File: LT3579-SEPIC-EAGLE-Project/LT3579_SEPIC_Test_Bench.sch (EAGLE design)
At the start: 3 parts, among them IC1 LT3579EFE#PBF

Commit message: Modified Schematic EAGLE
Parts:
- removed L1: MSD1278T-183MLD, SamacSys_Parts:MSD1278T-183MLD
- added C_1, C_IN_1, C_IN_2, C_OUT_1, C_OUT_2, C_OUT_3: CGA4J1X7R1E475K125AE, SamacSys_Parts:CGA4J1X7R1E475K125AE
- added C_C: CGA4F4C0G2W222J085AE, SamacSys_Parts:CGA4F4C0G2W222J085AE
- added C_F: CGA2B2C0G1H470J050BA, SamacSys_Parts:CGA2B2C0G1H470J050BA
- added C_SS: CGA4J2X8R1E224K125AE, SamacSys_Parts:CGA4J2X8R1E224K125AE
- added L1L2: MSD1278T-183MLD, SamacSys_Parts:MSD1278T-183MLD
- added R_C: AC0805JR-0712KL, SamacSys_Parts:AC0805JR-0712KL
- added R_T: AC0805FR-07124KL, SamacSys_Parts:AC0805FR-07124KL
- added R_UVLO2: RT1206BRD075KL, SamacSys_Parts:RT1206BRD075KL
- added U2: RQ5E050ATTCL, SamacSys_Parts:RQ5E050ATTCL
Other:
- note added: "LT3579 SEPIC Config: 13Vin -> 14Vout"
- moved on the sheet: D1
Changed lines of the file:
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@@
 <layer number="97" name="Info" color="7" fill="1" visible="yes" active="yes"/>
 <layer number="98" name="Guide" color="6" fill="1" visible="yes" active="yes"/>
+<layer number="99" name="SpiceOrder" color="7" fill="1" visible="yes" active="yes"/>
 </layers>
 <schematic xreflabel="%F%N/%S.%C%R" xrefpart="/%S.%C%R">
@@
 <parts>
 <part name="IC1" library="SamacSys_Parts" deviceset="LT3579EFE#PBF" device=""/>
-<part name="L1" library="SamacSys_Parts" deviceset="MSD1278T-183MLD" device=""/>
+<part name="L1L2" library="SamacSys_Parts" deviceset="MSD1278T-183MLD" device=""/>
 <part name="D1" library="SamacSys_Parts" deviceset="MBRS360T3G" device=""/>
+<part name="C_IN_1" library="SamacSys_Parts" deviceset="CGA4J1X7R1E475K125AE" device=""/>
+<part name="C_IN_2" library="SamacSys_Parts" deviceset="CGA4J1X7R1E475K125AE" device=""/>
+<part name="C_1" library="SamacSys_Parts" deviceset="CGA4J1X7R1E475K125AE" device=""/>
+<part name="X_1" library="ngspice-simulation" library_urn="urn:adsk.eagle:library:527439" deviceset="GND" device=""/>
+<part name="X_2" library="ngspice-simulation" library_urn="urn:adsk.eagle:library:527439" deviceset="GND" device=""/>
+<part name="C_OUT_1" library="SamacSys_Parts" deviceset="CGA4J1X7R1E475K125AE" device=""/>
+<part name="C_SS" library="SamacSys_Parts" deviceset="CGA4J2X8R1E224K125AE" device=""/>
+<part name="C_OUT_2" library="SamacSys_Parts" deviceset="CGA4J1X7R1E475K125AE" device=""/>
+<part name="C_OUT_3" library="SamacSys_Parts" deviceset="CGA4J1X7R1E475K125AE" device=""/>
+<part name="C_F" library="SamacSys_Parts" deviceset="CGA2B2C0G1H470J050BA" device=""/>
+<part name="C_C" library="SamacSys_Parts" deviceset="CGA4F4C0G2W222J085AE" device=""/>
+<part name="R_UVLO2" library="SamacSys_Parts" deviceset="RT1206BRD075KL" device=""/>
+<part name="R_T" library="SamacSys_Parts" deviceset="AC0805FR-07124KL" device=""/>
+<part name="R_C" library="SamacSys_Parts" deviceset="AC0805JR-0712KL" device=""/>
+<part name="U2" library="SamacSys_Parts" deviceset="RQ5E050ATTCL" device=""/>
 </parts>
 <sheets>
 <sheet>
 <plain>
+<text x="-40.64" y="53.34" size="1.778" layer="91">LT3579 SEPIC Config: 13Vin -&gt; 14Vout</text>
 </plain>
 <instances>
@@
 <attribute name="VALUE" x="13.97" y="17.78" size="1.778" layer="96" align="center-left"/>
 </instance>
-<instance part="L1" gate="G$1" x="-60.96" y="22.86" smashed="yes">
-<attribute name="NAME" x="-44.45" y="30.48" size="1.778" layer="95" align="center-left"/>
-<attribute name="VALUE" x="-44.45" y="27.94" size="1.778" layer="96" align="center-left"/>
+<instance part="L1L2" gate="G$1" x="-58.42" y="38.1" smashed="yes">
+<attribute name="NAME" x="-41.91" y="45.72" size="1.778" layer="95" align="center-left"/>
+<attribute name="VALUE" x="-41.91" y="43.18" size="1.778" layer="96" align="center-left"/>
 </instance>
-<instance part="D1" gate="G$1" x="58.42" y="38.1" smashed="yes" rot="R180">
-<attribute name="NAME" x="46.99" y="33.02" size="1.778" layer="95" rot="R180" align="center-left"/>
-<attribute name="VALUE" x="46.99" y="35.56" size="1.778" layer="96" rot="R180" align="center-left"/>
+<instance part="D1" gate="G$1" x="50.8" y="53.34" smashed="yes" rot="R180">
+<attribute name="NAME" x="39.37" y="48.26" size="1.778" layer="95" rot="R180" align="center-left"/>
+<attribute name="VALUE" x="39.37" y="50.8" size="1.778" layer="96" rot="R180" align="center-left"/>
+</instance>
+<instance part="C_IN_1" gate="G$1" x="-55.88" y="-12.7" smashed="yes" rot="R90">
+<attribute name="NAME" x="-62.23" y="-3.81" size="1.778" layer="95" rot="R90" align="center-left"/>
+<attribute name="VALUE" x="-59.69" y="-3.81" size="1.778" layer="96" rot="R90" align="center-left"/>
+</instance>
+<instance part="C_IN_2" gate="G$1" x="-68.58" y="-12.7" smashed="yes" rot="R90">
+<attribute name="NAME" x="-74.93" y="-3.81" size="1.778" layer="95" rot="R90" align="center-left"/>
+<attribute name="VALUE" x="-72.39" y="-3.81" size="1.778" layer="96" rot="R90" align="center-left"/>
+</instance>
+<instance part="C_1" gate="G$1" x="55.88" y="27.94" smashed="yes" rot="R180">
+<attribute name="NAME" x="46.99" y="21.59" size="1.778" layer="95" rot="R180" align="center-left"/>
+<attribute name="VALUE" x="46.99" y="24.13" size="1.778" layer="96" rot="R180" align="center-left"/>
+</instance>
+<instance part="X_1" gate="G$1" x="-68.58" y="-17.78" smashed="yes"/>
+<instance part="X_2" gate="G$1" x="-55.88" y="-17.78" smashed="yes"/>
+<instance part="C_OUT_1" gate="G$1" x="81.28" y="15.24" smashed="yes" rot="R90">
+<attribute name="NAME" x="74.93" y="24.13" size="1.778" layer="95" rot="R90" align="center-left"/>
+<attribute name="VALUE" x="77.47" y="24.13" size="1.778" layer="96" rot="R90" align="center-left"/>
+</instance>
+<instance part="C_SS" gate="G$1" x="58.42" y="-25.4" smashed="yes" rot="R90">
+<attribute name="NAME" x="52.07" y="-16.51" size="1.778" layer="95" rot="R90" align="center-left"/>
+<attribute name="VALUE" x="54.61" y="-16.51" size="1.778" layer="96" rot="R90" align="center-left"/>
+</instance>
+<instance part="C_OUT_2" gate="G$1" x="96.52" y="15.24" smashed="yes" rot="R90">
+<attribute name="NAME" x="90.17" y="24.13" size="1.778" layer="95" rot="R90" align="center-left"/>
+<attribute name="VALUE" x="92.71" y="24.13" size="1.778" layer="96" rot="R90" align="center-left"/>
+</instance>
+<instance part="C_OUT_3" gate="G$1" x="111.76" y="15.24" smashed="yes" rot="R90">
+<attribute name="NAME" x="105.41" y="24.13" size="1.778" layer="95" rot="R90" align="center-left"/>
+<attribute name="VALUE" x="107.95" y="24.13" size="1.778" layer="96" rot="R90" align="center-left"/>
+</instance>
+<instance part="C_F" gate="G$1" x="81.28" y="-15.24" smashed="yes" rot="R270">
+<attribute name="NAME" x="87.63" y="-24.13" size="1.778" layer="95" rot="R270" align="center-left"/>
+<attribute name="VALUE" x="85.09" y="-24.13" size="1.778" layer="96" rot="R270" align="center-left"/>
+</instance>
+<instance part="C_C" gate="G$1" x="86.36" y="-5.08" smashed="yes">
+<attribute name="NAME" x="95.25" y="1.27" size="1.778" layer="95" align="center-left"/>
+<attribute name="VALUE" x="95.25" y="-1.27" size="1.778" layer="96" align="center-left"/>
+</instance>
+<instance part="R_UVLO2" gate="G$1" x="104.14" y="-53.34" smashed="yes" rot="R90">
+<attribute name="NAME" x="97.79" y="-39.37" size="1.778" layer="95" rot="R90" align="center-left"/>
+<attribute name="VALUE" x="100.33" y="-39.37" size="1.778" layer="96" rot="R90" align="center-left"/>
+</instance>
+<instance part="R_T" gate="G$1" x="119.38" y="-50.8" smashed="yes" rot="R90">
+<attribute name="NAME" x="113.03" y="-36.83" size="1.778" layer="95" rot="R90" align="center-left"/>
+<attribute name="VALUE" x="115.57" y="-36.83" size="1.778" layer="96" rot="R90" align="center-left"/>
+</instance>
+<instance part="R_C" gate="G$1" x="134.62" y="-50.8" smashed="yes" rot="R90">
+<attribute name="NAME" x="128.27" y="-36.83" size="1.778" layer="95" rot="R90" align="center-left"/>
+<attribute name="VALUE" x="130.81" y="-36.83" size="1.778" layer="96" rot="R90" align="center-left"/>
+</instance>
+<instance part="U2" gate="G$1" x="33.02" y="-40.64" smashed="yes">
+<attribute name="NAME" x="44.45" y="-36.83" size="1.778" layer="95" align="center-left"/>
+<attribute name="VALUE" x="44.45" y="-39.37" size="1.778" layer="96" align="center-left"/>
 </instance>
 </instances>
@@
 </schematic>
 </drawing>
+<compatibility>
+<note version="8.2" severity="warning">
+Since Version 8.2, EAGLE supports online libraries. The ids
+of those online libraries will not be understood (or retained)
+with this version.
+</note>
+<note version="8.3" severity="warning">
+Since Version 8.3, EAGLE supports URNs for individual library
+assets (packages, symbols, and devices). The URNs of those assets
+will not be understood (or retained) with this version.
+</note>
+</compatibility>
 </eagle>

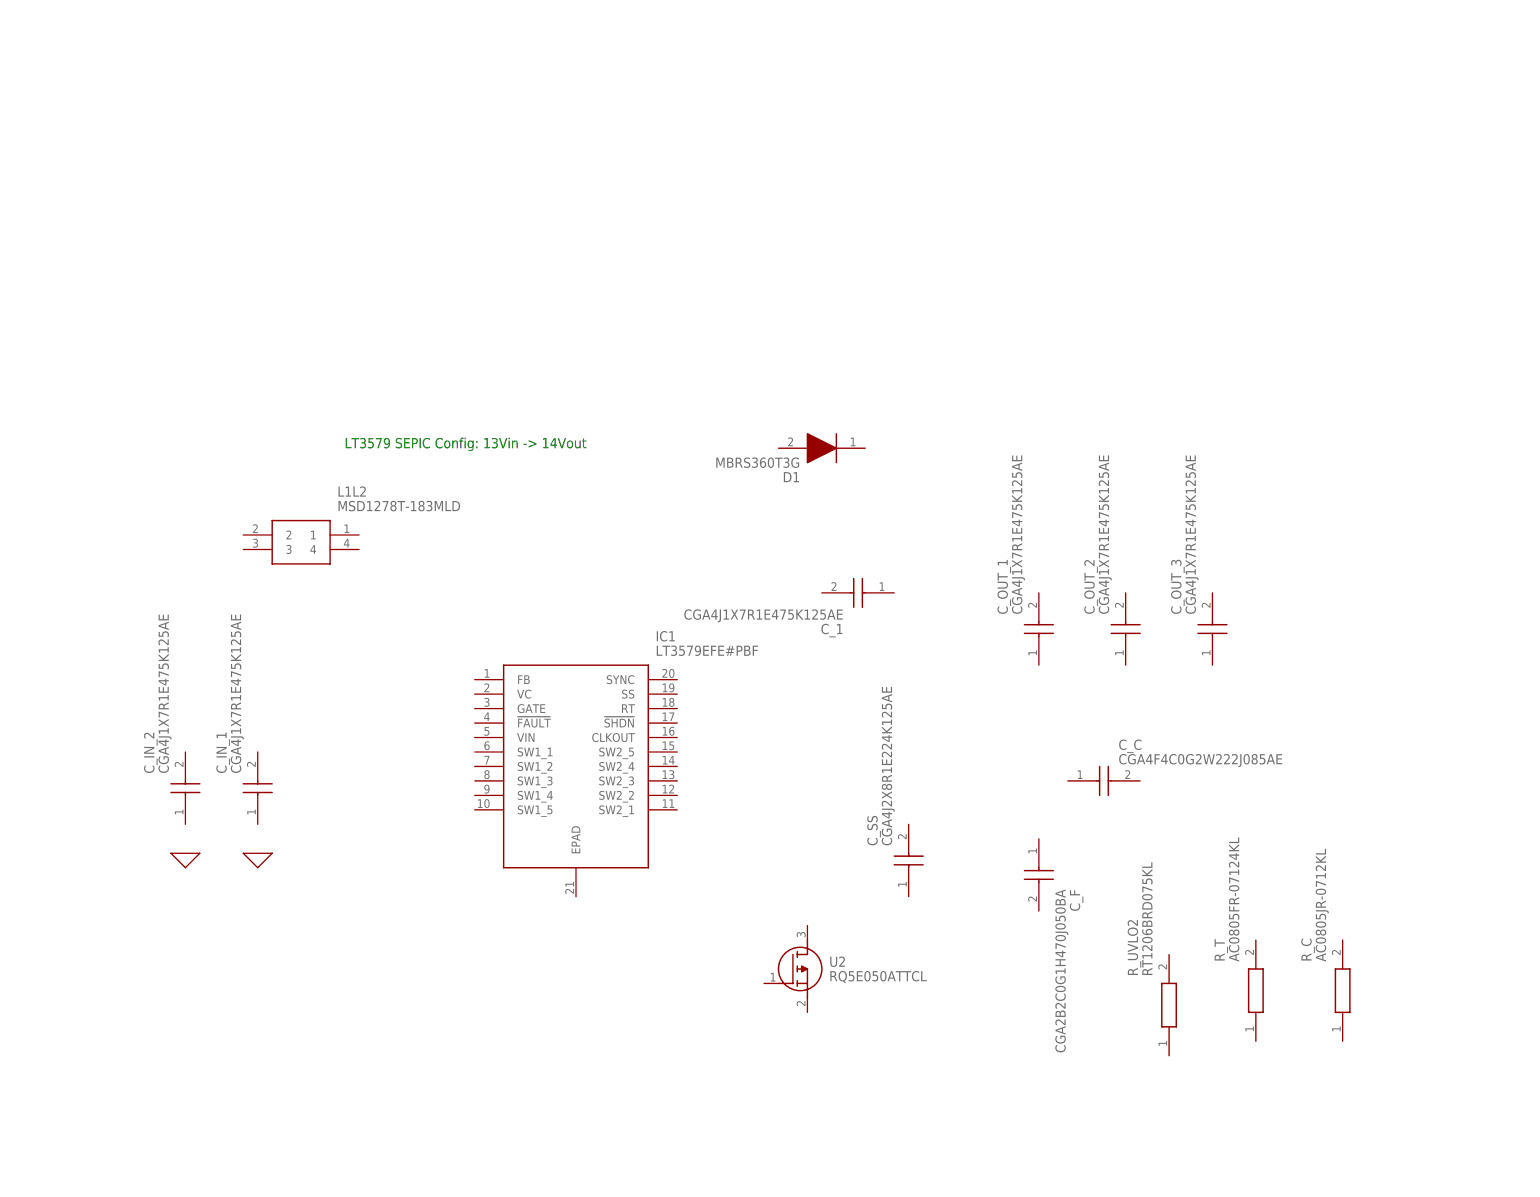
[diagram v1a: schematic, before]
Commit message: Added New Libraries and modified schematic
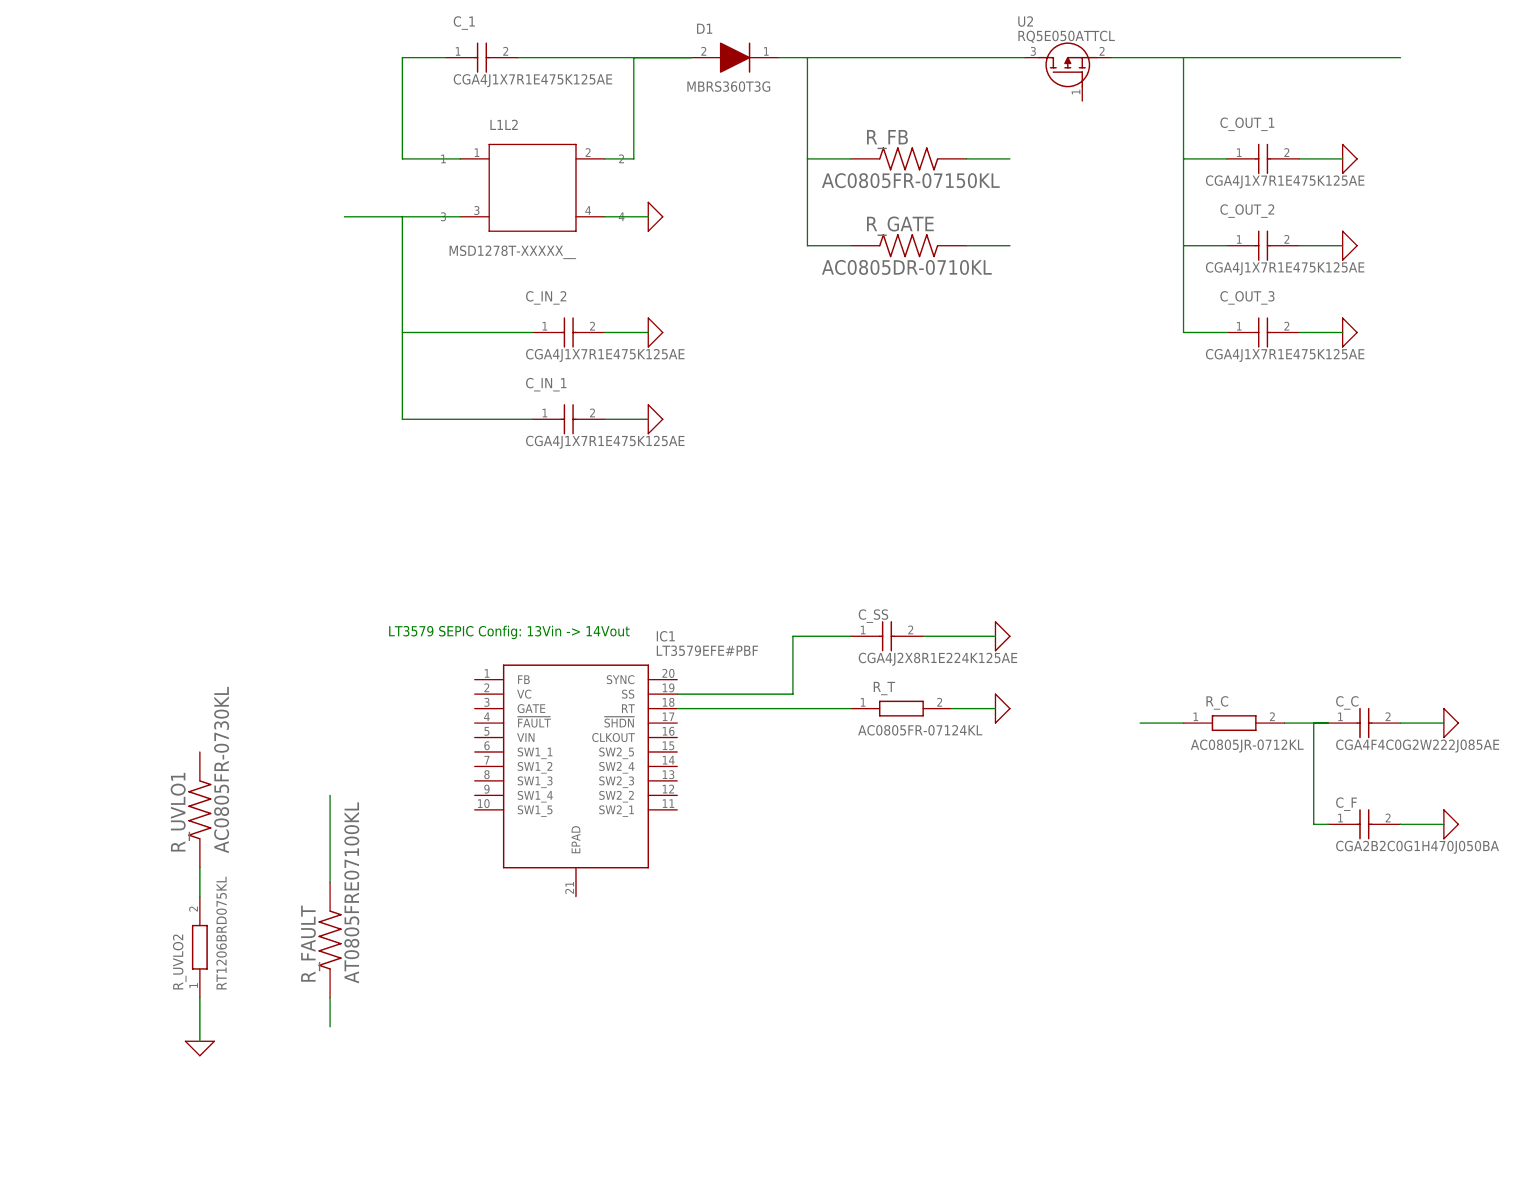
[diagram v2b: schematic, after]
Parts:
- added R_FAULT: AT0805FRE07100KL, AT0805FRE07100KL:AT0805FRE07100KL
- added R_FB: AC0805FR-07150KL, AC0805FR-07150KL:AC0805FR-07150KL
- added R_GATE: AC0805DR-0710KL, AC0805DR-0710KL:AC0805DR-0710KL
- added R_UVLO1: AC0805FR-0730KL, AC0805FR-0730KL:AC0805FR-0730KL
- L1L2: value MSD1278T-183MLD -> MSD1278T-XXXXX__; device SamacSys_Parts:MSD1278T-183MLD -> MSD1278T-Series:MSD1278T-XXXXX__
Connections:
- new net 0: C_C.2, C_F.2, C_IN_1.2, C_IN_2.2, C_OUT_1.2, C_OUT_2.2, C_OUT_3.2, C_SS.2, R_T.2, R_UVLO2.1
- new net FAULT: R_FAULT.1
- new net N$1: R_UVLO1.1, R_UVLO2.2
- new net N$10: C_IN_1.1, C_IN_2.1
- new net N$11: R_FB.2
- new net N$13: D1.K, R_FB.1, R_GATE.1, U2.D
- new net N$14: C_SS.1, IC1.SS
- new net N$2: R_FAULT.2
- new net N$3: R_GATE.2
- new net N$4: C_C.1, C_F.1, R_C.2
- new net N$5: C_1.1
- new net N$6: C_OUT_1.1, C_OUT_2.1, C_OUT_3.1, U2.S
- new net N$7: R_C.1
- new net N$8: IC1.RT, R_T.1
- new net N$9: C_1.2, D1.A
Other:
- moved on the sheet: C_1, C_C, C_F, C_IN_1, C_IN_2, C_OUT_1, C_OUT_2, C_OUT_3, C_SS, D1, L1L2, R_C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
